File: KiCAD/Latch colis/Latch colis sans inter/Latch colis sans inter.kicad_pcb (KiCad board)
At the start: 2 copper layers, 80.5 x 56 mm, 8 parts, among them J1 KF301-2P, J4 Jauges, Q1 2N2222A, Q2 BS250, U1 Heltec_LoRa32_V2_RST_side, U2 Module HX711

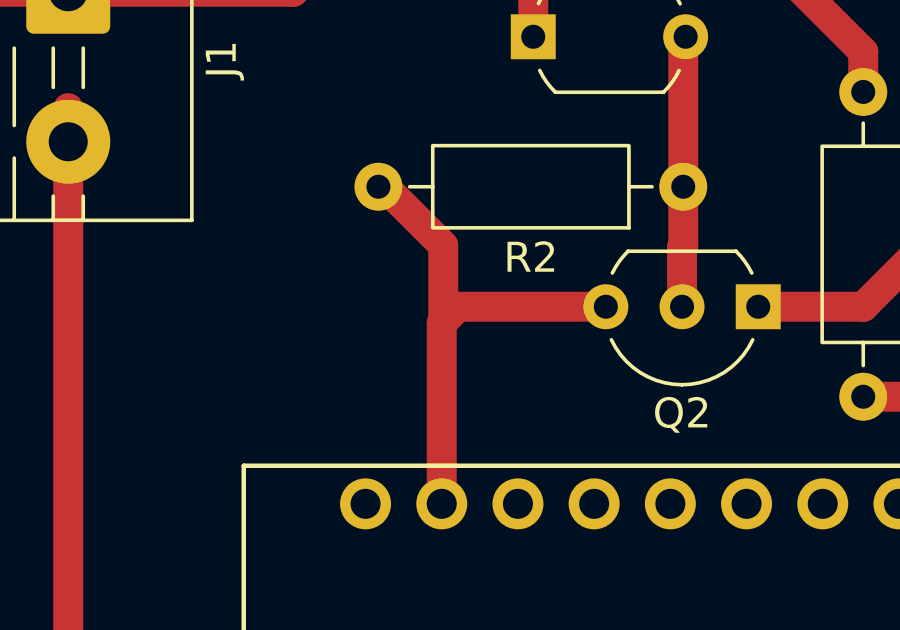
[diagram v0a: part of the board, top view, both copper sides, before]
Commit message: Nettoyage ERC (no_connect) et reduction connecteur J4 a 4 broches
Suite a l'abandon des contacts de porte (design "sans inter"), les 2
signaux en trop du connecteur J4 n'ont plus lieu d'etre.

Co-Authored-By: Claude Sonnet 5 <noreply@anthropic.com>
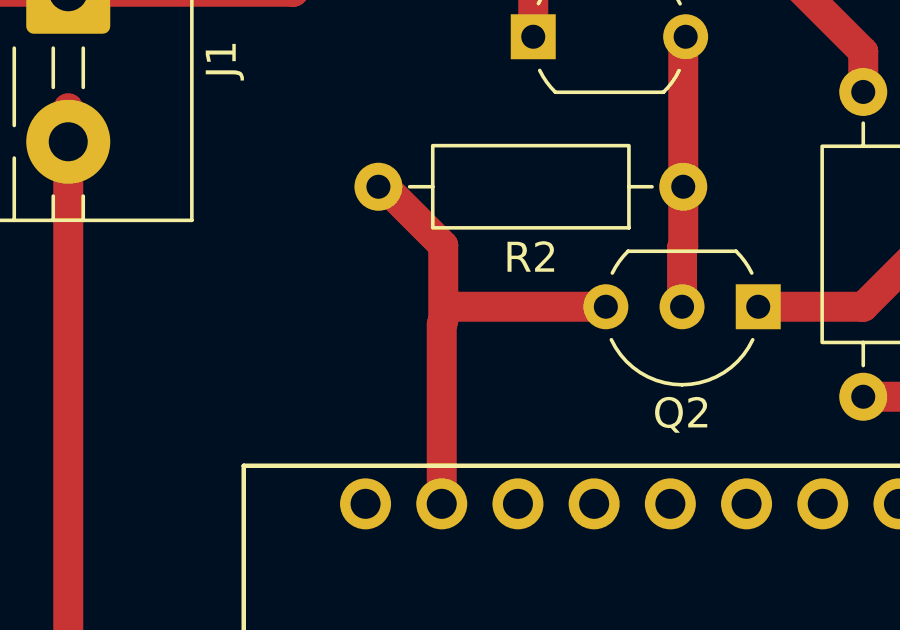
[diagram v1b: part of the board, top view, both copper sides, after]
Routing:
- net /+3.3V HX711: track 17.2 -> 16.5 mm
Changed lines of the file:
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@@
 		)
 		(embedded_fonts no)
-		(model "${MODEL3D_DIR}/KF301-5.0-2P.step"
+		(model "C:/Users/floph/Dropbox/Dossier de l’équipe Philippe DAVID/Programme VS code/Mes empreintes.3dshapes/KF301-5.0-2P.step"
 			(offset
 				(xyz 2.5 0 0)
@@
 		)
 		(embedded_fonts no)
-		(model "${KICAD10_3RD_PARTY}/HX711.step"
-			(opacity 0.7000)
+		(model "C:/Users/floph/Dropbox/Dossier de l’équipe Philippe DAVID/Programme VS code/Mes empreintes.3dshapes/HX711 Breakout v7.step"
 			(offset
-				(xyz 18 9 4)
+				(xyz 0.5 -1 2.5)
 			)
 			(scale
@@
 		)
 		(embedded_fonts no)
-		(model "${KICAD10_3RD_PARTY}/MODULE_ESP32_LORA_V2.0.step"
+		(model "C:/Users/floph/Dropbox/Dossier de l’équipe Philippe DAVID/Programme VS code/Mes empreintes.3dshapes/MODULE_ESP32_LORA_V2.0.step"
 			(offset
 				(xyz 0 -1.5 2.5)
@@
 		(width 1)
 		(layer "F.Cu")
-		(net "/+3.3V HX711")
-	)
-	(segment
-		(start 78.45 65.55)
-		(end 79 65)
-		(width 1)
-		(layer "F.Cu")

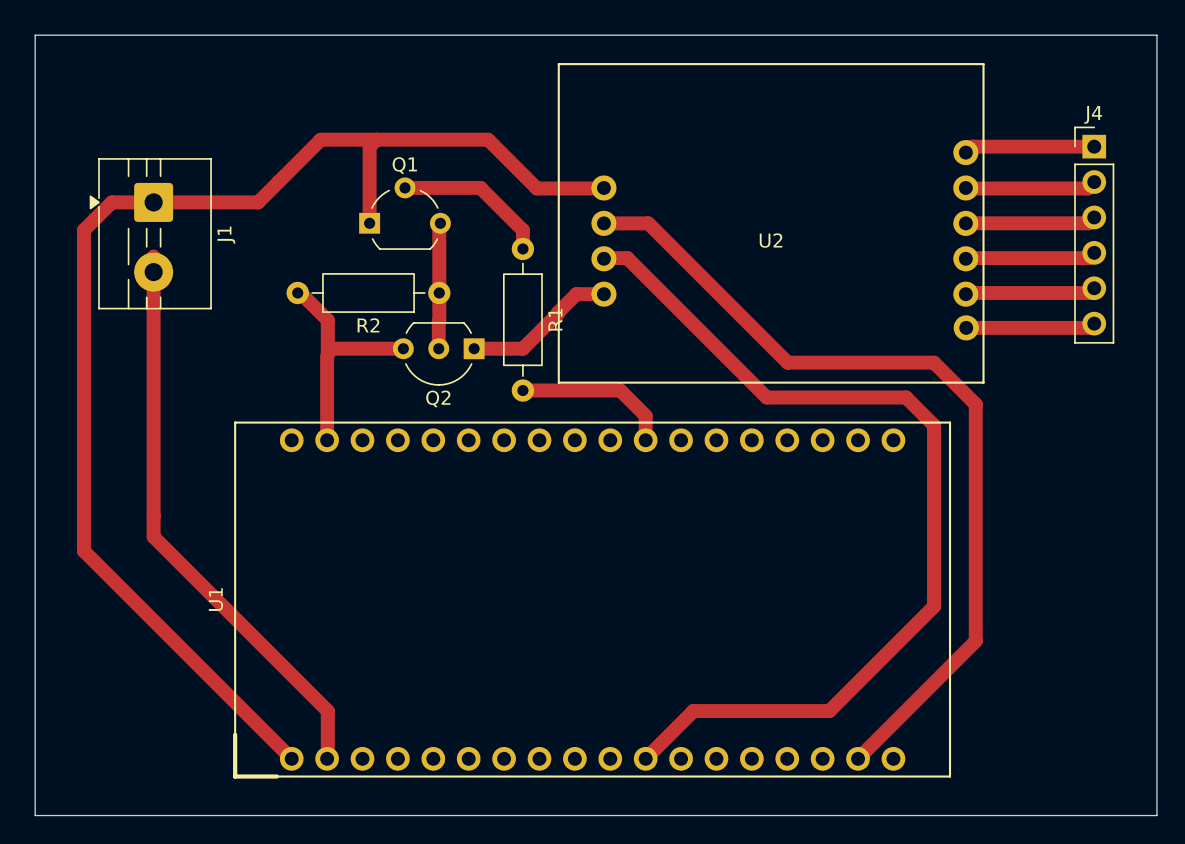
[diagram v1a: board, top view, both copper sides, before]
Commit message: Restaure la veille RTC (regressee par la fusion) et ajoute la correction d'horloge via le recepteur
- courrier_emetteur.rs : restauration de la version deep-sleep RTC/sans
  contact de porte (la fusion precedente avait reintroduit par erreur
  l'ancienne version a relais). Envoie desormais "RIEN" a chaque reveil sans
  poids (au lieu de rien), pour toujours declencher l'echange ACK.
- courrier_recepteur.rs : connexion Wi-Fi + NTP (non bloquante), calcule a
  chaque reception le nombre de secondes jusqu'au prochain 12h00/18h00 (heure
  de Paris) et le glisse a la fin de l'ACK.
- courrier_emetteur.rs : utilise cette correction comme duree de deep-sleep
  au lieu de l'intervalle fixe de 12h, avec repli sur l'intervalle par defaut
  si aucun ACK/correction n'est recu.
- Nouveaux modules src/temps.rs (conversion UTC->Paris, calcul du prochain
  reveil) et src/wifi.rs (connexion, repris du projet piscine).
- src/config.rs (gitignore) + config.example.rs : identifiants Wi-Fi du
  recepteur, jamais commites (depot public).

Co-Authored-By: Claude Sonnet 5 <noreply@anthropic.com>
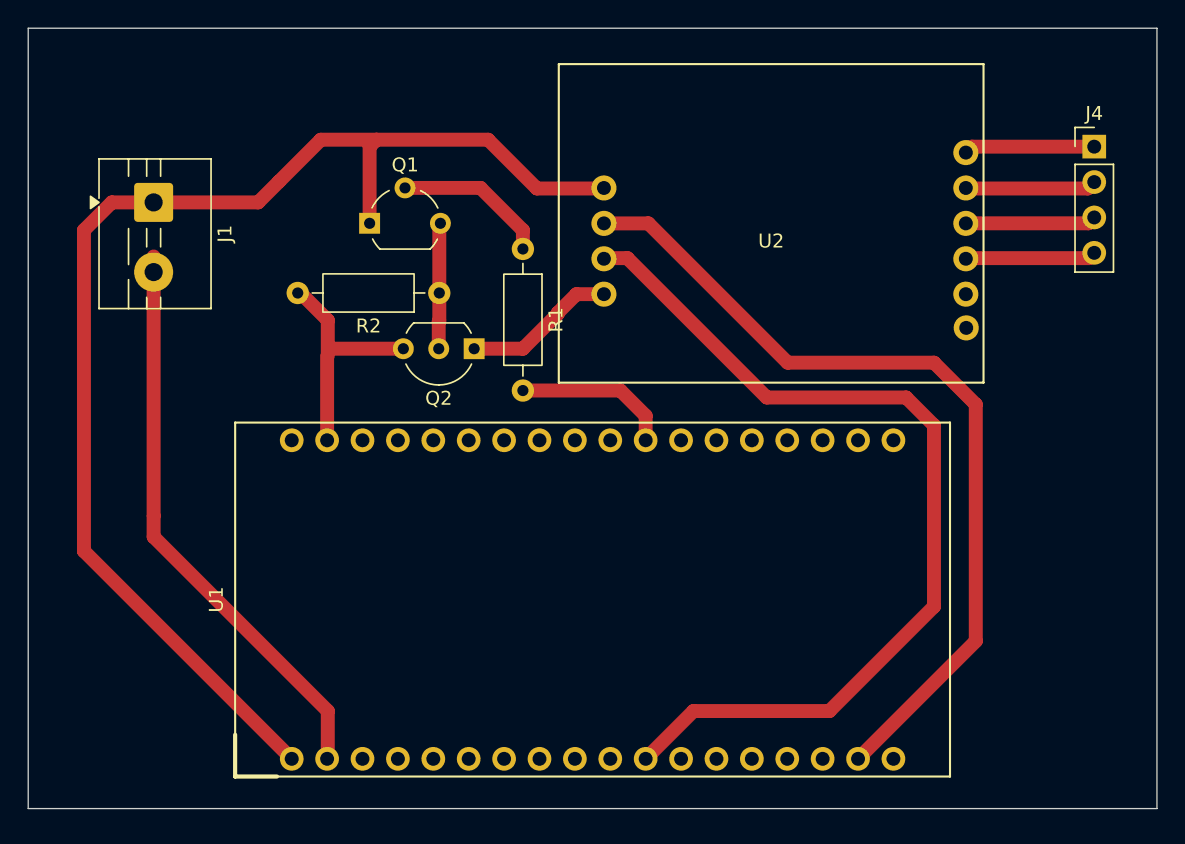
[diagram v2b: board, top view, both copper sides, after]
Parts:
- J4: footprint Connector_PinHeader_2.54mm:PinHeader_1x06_P2.54mm_Vertical -> Connector_PinHeader_2.54mm:PinHeader_1x04_P2.54mm_Vertical
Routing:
- net Net-(J4-Pin_6): track 9.31 -> 0.00 mm
- net Net-(J4-Pin_5): track 9.39 -> 0.12 mm
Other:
- board size 80.5 x 56 mm -> 81 x 56 mm
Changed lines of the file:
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@@
 		)
 	)
-	(footprint "Connector_PinHeader_2.54mm:PinHeader_1x06_P2.54mm_Vertical"
+	(footprint "Connector_PinHeader_2.54mm:PinHeader_1x04_P2.54mm_Vertical"
 		(layer "F.Cu")
 		(at 133.5 50.5)
-		(descr "Through hole straight pin header, 1x06, 2.54mm pitch, single row")
-		(tags "Through hole pin header THT 1x06 2.54mm single row")
+		(descr "Through hole straight pin header, 1x04, 2.54mm pitch, single row")
+		(tags "Through hole pin header THT 1x04 2.54mm single row")
 		(property "Reference" "J4"
 			(at 0 -2.38 0)
@@
 		)
 		(property "Value" "Jauges"
-			(at 0 15.08 0)
+			(at 0 10 0)
 			(layer "F.Fab")
 			(effects
@@
 		(fp_line
 			(start -1.38 1.27)
-			(end -1.38 14.08)
+			(end -1.38 9)
 			(stroke
 				(width 0.12)
@@
 		)
 		(fp_line
-			(start -1.38 14.08)
-			(end 1.38 14.08)
+			(start -1.38 9)
+			(end 1.38 9)
 			(stroke
 				(width 0.12)
@@
 		(fp_line
 			(start 1.38 1.27)
-			(end 1.38 14.08)
+			(end 1.38 9)
 			(stroke
 				(width 0.12)
@@
 		(fp_rect
 			(start -1.77 -1.77)
-			(end 1.77 14.47)
+			(end 1.77 9.39)
 			(stroke
 				(width 0.05)
@@
 		)
 		(fp_line
-			(start -1.27 13.97)
+			(start -1.27 8.89)
 			(end -1.27 -0.635)
 			(stroke
@@
 		(fp_line
 			(start 1.27 -1.27)
-			(end 1.27 13.97)
-			(stroke
-				(width 0.1)
-				(type solid)
-			)
-			(layer "F.Fab")
-		)
-		(fp_line
-			(start 1.27 13.97)
-			(end -1.27 13.97)
+			(end 1.27 8.89)
+			(stroke
+				(width 0.1)
+				(type solid)
+			)
+			(layer "F.Fab")
+		)
+		(fp_line
+			(start 1.27 8.89)
+			(end -1.27 8.89)
 			(stroke
 				(width 0.1)
@@
 		)
 		(fp_text user "${REFERENCE}"
-			(at 0 6.35 90)
+			(at 0 3.81 90)
 			(layer "F.Fab")
 			(effects
@@
 			(pintype "passive")
 		)
-		(pad "5" thru_hole circle
-			(at 0 10.16)
-			(size 1.7 1.7)
-			(drill 1)
-			(layers "*.Cu" "*.Mask")
-			(remove_unused_layers no)
-			(net "Net-(J4-Pin_5)")
-			(pinfunction "Pin_5_5")
-			(pintype "passive")
-		)
-		(pad "6" thru_hole circle
-			(at 0 12.7)
-			(size 1.7 1.7)
-			(drill 1)
-			(layers "*.Cu" "*.Mask")
-			(remove_unused_layers no)
-			(net "Net-(J4-Pin_6)")
-			(pinfunction "Pin_6_6")
-			(pintype "passive")
-		)
 		(embedded_fonts no)
-		(model "${KICAD10_3DMODEL_DIR}/Connector_PinHeader_2.54mm.3dshapes/PinHeader_1x06_P2.54mm_Vertical.step"
+		(model "${KICAD10_3DMODEL_DIR}/Connector_PinHeader_2.54mm.3dshapes/PinHeader_1x04_P2.54mm_Vertical.step"
 			(offset
 				(xyz 0 0 0)
@@
 	)
 	(gr_rect
-		(start 57.5 42.5)
-		(end 138 98.5)
+		(start 57 42)
+		(end 138 98)
 		(stroke
 			(width 0.05)
@@
 	)
 	(segment
-		(start 124.37 61)
-		(end 133.16 61)
-		(width 1)
-		(layer "F.Cu")
-		(net "Net-(J4-Pin_5)")
-	)
-	(segment
 		(start 124.285 61.085)
 		(end 124.37 61)
@@
 	)
 	(segment
-		(start 133.16 61)
-		(end 133.5 60.66)
-		(width 1)
-		(layer "F.Cu")
-		(net "Net-(J4-Pin_5)")
-	)
-	(segment
-		(start 133.195 63.505)
-		(end 133.5 63.2)
-		(width 1)
-		(layer "F.Cu")
-		(net "Net-(J4-Pin_6)")
-	)
-	(segment
-		(start 124.315 63.505)
-		(end 133.195 63.505)
-		(width 1)
-		(layer "F.Cu")
-		(net "Net-(J4-Pin_6)")
-	)
-	(segment
